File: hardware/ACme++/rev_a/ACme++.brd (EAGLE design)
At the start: 72.6 x 47.1 mm, 90 parts, among them J1 AC-PLUG, J2 WIRE_HOLE-14AWG, J3 TC2030-CTX-NL, J4 WIRE_HOLE-14AWG, J5 WIRE_HOLE-14AWG, K1 S216S01F, Q1 STGD5NB120SZT4, Q2 FDV301N, U1 ADE7753, U2 SR086SG-G, U3 TDA3664AT, U4 FM25LBTDFN-8, U5 CC2538, U6 DS2411, U7 TXB0104RGY, X1 ECS-35-17-5PX-TR, X2 EPSON-FA-128, X3 FC-12M32.7680KA-A3

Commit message: thinking about ac lines, tantalum caps
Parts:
- moved R14 0.13 mm to (46.7, 32.4)
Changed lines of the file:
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@@
 <layer number="27" name="tValues" color="7" fill="1" visible="no" active="yes"/>
 <layer number="28" name="bValues" color="7" fill="1" visible="no" active="yes"/>
-<layer number="29" name="tStop" color="7" fill="3" visible="no" active="yes"/>
+<layer number="29" name="tStop" color="7" fill="3" visible="yes" active="yes"/>
 <layer number="30" name="bStop" color="7" fill="6" visible="no" active="yes"/>
 <layer number="31" name="tCream" color="7" fill="4" visible="no" active="yes"/>
@@
 <wire x1="71.247" y1="33.909" x2="71.247" y2="36.83" width="0.254" layer="21"/>
 <wire x1="71.247" y1="36.83" x2="68.453" y2="36.83" width="0.254" layer="21"/>
-<text x="61.976" y="26.924" size="1.27" layer="21" font="vector" ratio="12" rot="SR270" align="top-center">N</text>
-<text x="61.976" y="19.939" size="1.27" layer="21" font="vector" ratio="12" rot="SR270" align="top-center">P</text>
+<text x="63.881" y="26.924" size="1.27" layer="21" font="vector" ratio="12" rot="SR270" align="top-center">N</text>
+<text x="63.881" y="19.939" size="1.27" layer="21" font="vector" ratio="12" rot="SR270" align="top-center">P</text>
+<polygon width="0" layer="29" spacing="0.254" pour="hatch">
+<vertex x="40.132" y="28.321"/>
+<vertex x="45.974" y="28.321"/>
+<vertex x="48.895" y="31.242"/>
+<vertex x="55.372" y="31.242"/>
+<vertex x="62.103" y="24.511"/>
+<vertex x="62.103" y="18.923"/>
+<vertex x="60.325" y="18.923"/>
+<vertex x="60.198" y="18.923"/>
+<vertex x="60.198" y="23.876"/>
+<vertex x="54.61" y="29.464"/>
+<vertex x="49.657" y="29.464"/>
+<vertex x="46.736" y="26.543"/>
+<vertex x="40.132" y="26.543"/>
+</polygon>
+<polygon width="0" layer="29" spacing="0.254" pour="hatch">
+<vertex x="39.243" y="32.512"/>
+<vertex x="39.243" y="37.973"/>
+<vertex x="43.561" y="42.291"/>
+<vertex x="44.831" y="41.021"/>
+<vertex x="41.021" y="37.211"/>
+<vertex x="41.021" y="32.512"/>
+<vertex x="39.37" y="32.512"/>
+</polygon>
 </plain>
 <attributes>
@@
 <element name="R12" library="SparkFun-Resistors" package="0805" value="1k" x="57.023" y="32.004" smashed="yes" rot="R270">
 <attribute name="DIGIKEY" value="P16058CT-ND" x="57.023" y="32.004" size="1.778" layer="27" rot="R270" display="off"/>
-<attribute name="NAME" x="57.5945" y="29.337" size="1.016" layer="25" font="vector" ratio="12" rot="R90" align="bottom-center"/>
+<attribute name="NAME" x="55.753" y="31.623" size="1.016" layer="25" font="vector" ratio="12" rot="R270" align="center-right"/>
 <attribute name="VALUE" x="55.626" y="33.02" size="0.4064" layer="27" rot="R270"/>
 </element>
@@
 <element name="C13" library="SparkFun-Passives" package="0805" value="33nF" x="58.801" y="32.004" smashed="yes" rot="R90">
 <attribute name="DIGIKEY" value="478-1389-1-ND" x="58.801" y="32.004" size="1.778" layer="27" rot="R90" display="off"/>
-<attribute name="NAME" x="59.3725" y="29.337" size="1.016" layer="25" font="vector" ratio="12" rot="R90" align="bottom-center"/>
+<attribute name="NAME" x="60.071" y="31.242" size="1.016" layer="25" font="vector" ratio="12" rot="R270" align="center-right"/>
 <attribute name="VALUE" x="60.198" y="30.988" size="0.4064" layer="27" rot="R90"/>
 </element>
 <element name="C22" library="SparkFun-Passives" package="0805" value="33nF" x="36.195" y="40.259" smashed="yes">
 <attribute name="DIGIKEY" value="478-1389-1-ND" x="36.195" y="40.259" size="1.778" layer="27" display="off"/>
-<attribute name="NAME" x="34.925" y="38.5445" size="1.016" layer="25" font="vector" ratio="12"/>
+<attribute name="NAME" x="36.195" y="39.5605" size="1.016" layer="25" font="vector" ratio="12" align="top-center"/>
 <attribute name="VALUE" x="35.179" y="38.862" size="0.4064" layer="27"/>
 </element>
 <element name="L4" library="powercube" package="35F0102" value="35F0121-0SR-10" x="51.308" y="33.02" smashed="yes" rot="R180">
 <attribute name="DIGIKEY" value="240-2520-1-ND" x="51.308" y="33.02" size="1.778" layer="27" rot="R180" display="off"/>
-<attribute name="NAME" x="51.308" y="31.115" size="1.016" layer="25" font="vector" ratio="12" rot="R180" align="bottom-center"/>
+<attribute name="NAME" x="51.308" y="34.671" size="1.016" layer="25" font="vector" ratio="12" align="bottom-center"/>
 <attribute name="VALUE" x="51.308" y="36.195" size="1.016" layer="27" font="vector" ratio="12" rot="R180" align="bottom-center"/>
 </element>
-<element name="R14" library="SparkFun-Resistors" package="0805" value="499k" x="46.736" y="32.512" smashed="yes" rot="R270">
-<attribute name="DIGIKEY" value="P499KCCT-ND" x="46.736" y="32.512" size="1.778" layer="27" rot="R270" display="off"/>
-<attribute name="NAME" x="47.3075" y="29.972" size="1.016" layer="25" font="vector" ratio="12" rot="R90" align="bottom-center"/>
-<attribute name="VALUE" x="45.339" y="33.528" size="0.4064" layer="27" rot="R270"/>
+<element name="R14" library="SparkFun-Resistors" package="0805" value="499k" x="46.736" y="32.385" smashed="yes" rot="R270">
+<attribute name="DIGIKEY" value="P499KCCT-ND" x="46.736" y="32.385" size="1.778" layer="27" rot="R270" display="off"/>
+<attribute name="NAME" x="45.593" y="31.115" size="1.016" layer="25" font="vector" ratio="12" rot="R270" align="center-right"/>
+<attribute name="VALUE" x="45.339" y="33.401" size="0.4064" layer="27" rot="R270"/>
 </element>
 <element name="R15" library="SparkFun-Resistors" package="0603-RES" value="1k" x="44.577" y="32.385" smashed="yes" rot="R270">
 <attribute name="DIGIKEY" value="RHM1.00KADCT-ND" x="44.577" y="32.385" size="1.778" layer="27" rot="R270" display="off"/>
-<attribute name="NAME" x="45.085" y="29.718" size="1.016" layer="25" font="vector" ratio="12" rot="R90" align="bottom-center"/>
+<attribute name="NAME" x="44.577" y="31.115" size="1.016" layer="25" font="vector" ratio="12" rot="R90" align="center-right"/>
 <attribute name="VALUE" x="43.434" y="33.401" size="0.4064" layer="27" font="vector" rot="R270"/>
 </element>
 <element name="C23" library="SparkFun-Passives" package="0805" value="33nF" x="42.545" y="32.385" smashed="yes" rot="R90">
 <attribute name="DIGIKEY" value="478-1389-1-ND" x="42.545" y="32.385" size="1.778" layer="27" rot="R90" display="off"/>
-<attribute name="NAME" x="43.1165" y="29.845" size="1.016" layer="25" font="vector" ratio="12" rot="R90" align="bottom-center"/>
+<attribute name="NAME" x="42.545" y="31.115" size="1.016" layer="25" font="vector" ratio="12" rot="R90" align="center-right"/>
 <attribute name="VALUE" x="43.942" y="31.369" size="0.4064" layer="27" rot="R90"/>
 </element>
@@
 <wire x1="31.623" y1="38.227" x2="31.328" y2="37.932" width="0.4064" layer="1"/>
 <wire x1="31.328" y1="37.932" x2="29.535" y2="37.932" width="0.4064" layer="1"/>
-<wire x1="46.736" y1="31.612" x2="46.659" y2="31.535" width="0.762" layer="1"/>
-<wire x1="46.659" y1="31.535" x2="44.577" y2="31.535" width="0.762" layer="1"/>
 <wire x1="44.577" y1="31.535" x2="44.527" y2="31.485" width="0.762" layer="1"/>
 <wire x1="44.527" y1="31.485" x2="42.545" y2="31.485" width="0.762" layer="1"/>
@@
 <via x="32.893" y="38.227" extent="1-16" drill="0.254"/>
 <wire x1="32.893" y1="38.227" x2="31.623" y2="38.227" width="0.4064" layer="1"/>
+<wire x1="44.577" y1="31.535" x2="44.627" y2="31.485" width="0.762" layer="1"/>
+<wire x1="44.627" y1="31.485" x2="46.736" y2="31.485" width="0.762" layer="1"/>
 </signal>
 <signal name="!ADE_CS">
@@
 <contactref element="L4" pad="2"/>
 <contactref element="R14" pad="1"/>
-<wire x1="49.5173" y1="33.02" x2="49.1253" y2="33.412" width="0.762" layer="1"/>
-<wire x1="49.1253" y1="33.412" x2="46.736" y2="33.412" width="0.762" layer="1"/>
+<wire x1="49.5173" y1="33.02" x2="49.2523" y2="33.285" width="0.762" layer="1"/>
+<wire x1="49.2523" y1="33.285" x2="46.736" y2="33.285" width="0.762" layer="1"/>
 </signal>
 <signal name="EARTH_GND">

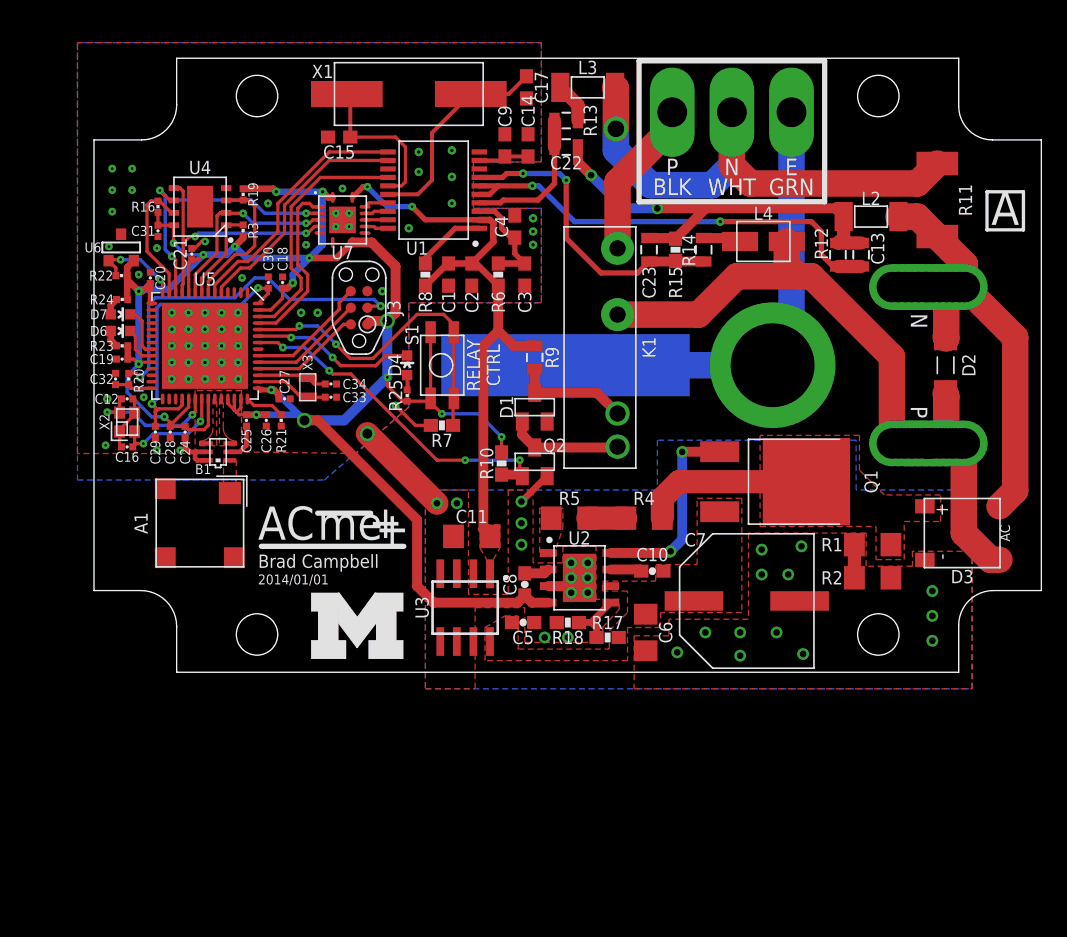
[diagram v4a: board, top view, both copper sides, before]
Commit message: routed ac under board, renamed
did my thing where part numbers correspond to values
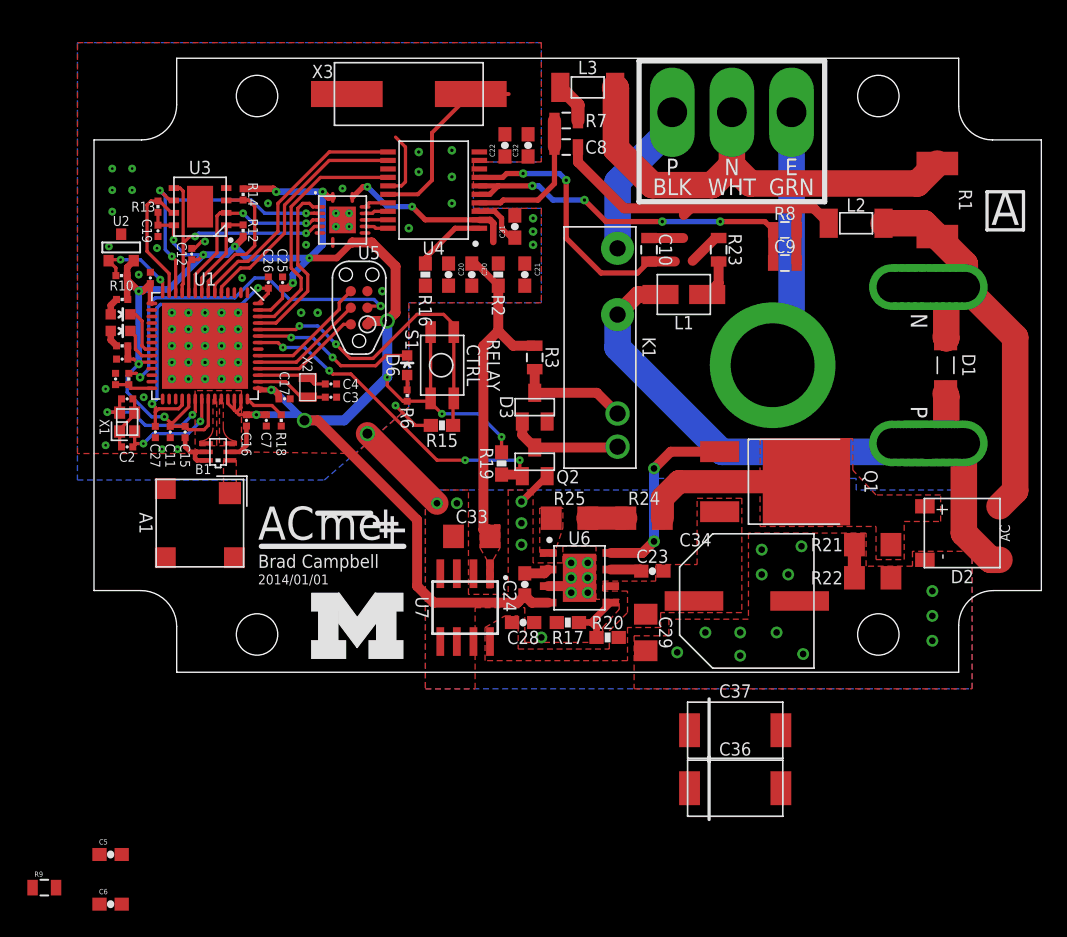
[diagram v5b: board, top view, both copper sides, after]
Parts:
- removed L4: 35F0121-0SR-10, powercube:35F0102
- added C36, C37: (no value), powercube:2917
- added L1: 35F0121-0SR-10, powercube:35F0102
- C1: value 0.1uF -> 12pF; device rcl:C0603 -> passives:0402_CAP
- C10, C8: value 0.1uF -> 33nF; device SparkFun-Passives:0603-CAP -> SparkFun-Passives:0805
- C11: value 47uF -> 0.1uF; device SparkFun-Passives:1206 -> passives:0402_CAP
- C12, C16: value 12pF -> 0.1uF
- C13: value 33nF -> 0.1uF; device SparkFun-Passives:0805 -> passives:0402_CAP
- C14: value 10uF -> 0.1uF; device rcl:C0603 -> passives:0402_CAP
- C15, C17: value 22pF -> 0.1uF; device rcl:C0603 -> passives:0402_CAP
- C18: value 1uF -> 0.1uF
- C2: value 10uF -> 12pF; device rcl:C0603 -> passives:0402_CAP
- C20, C21, C24: device passives:0402_CAP -> SparkFun-Passives:0603-CAP
- C22, C23: value 33nF -> 0.1uF; device SparkFun-Passives:0805 -> SparkFun-Passives:0603-CAP
- C25, C27: value 0.1uF -> 1uF
- C26: value 220pF -> 1uF
- C28: value 0.1uF -> 1uF; device passives:0402_CAP -> SparkFun-Passives:0603-CAP
- C29: device passives:0402_CAP -> SparkFun-Passives:1206
- C3: value 0.1uF -> 22pF; device rcl:C0603 -> passives:0402_CAP
- C30: value 1uF -> 10uF; device passives:0402_CAP -> SparkFun-Passives:0603-CAP
- C31: value 0.1uF -> 10uF; device passives:0402_CAP -> SparkFun-Passives:0603-CAP
- C32: value 1nF -> 10uF; device passives:0402_CAP -> SparkFun-Passives:0603-CAP
- C33: value 22pF -> 47uF; device passives:0402_CAP -> SparkFun-Passives:1206
- C34: value 22pF -> 470uF; device passives:0402_CAP -> powercube:CAP_SM_10MM
- C4: value 10uF -> 22pF; device rcl:C0603 -> passives:0402_CAP
- C5: value 1uF -> 22pF
- C6: value 1uF -> 22pF; device SparkFun-Passives:1206 -> SparkFun-Passives:0603-CAP
- C7: value 470uF -> 220pF; device powercube:CAP_SM_10MM -> passives:0402_CAP
- C9: value 0.1uF -> 33nF; device rcl:C0603 -> SparkFun-Passives:0805
- D1: value DIODE_MMBD914 -> SMAJ_TVS; device powercube:SOT-23 -> powercube:DO214_TVS
- D2: value SMAJ_TVS -> CD2320-BB11000; device powercube:DO214_TVS -> powercube:CD2320
- D3: value CD2320-BB11000 -> DIODE_MMBD914; device powercube:CD2320 -> powercube:SOT-23
- D4: value GREEN -> RED
- D6: value RED -> BLUE
- J2: value WIRE_HOLE-14AWG -> TC2030-CTX-NL; device powercube:WIRE_HOLE-14AWG -> connector:TC2030-IDC-NL
- J3: value TC2030-CTX-NL -> WIRE_HOLE-14AWG; device connector:TC2030-IDC-NL -> powercube:WIRE_HOLE-14AWG
- R1: value 200k -> 0.001; device SparkFun-Resistors:1206 -> SparkFun-Resistors:R2512
- R10: value 100k -> 2.2k; device SparkFun:0603-RES -> passives:0402_RES
- R11: value .001 -> 2.2k; device SparkFun-Resistors:R2512 -> passives:0402_RES
- R12, R13: value 1k -> 4.7k; device SparkFun-Resistors:0805 -> passives:0402_RES
- R14: value 499k -> 4.7k; device SparkFun-Resistors:0805 -> passives:0402_RES
- R15: value 1k -> 10k; device SparkFun-Resistors:0603-RES -> SparkFun:0603-RES
- R16: value 4.7k -> 10k; device passives:0402_RES -> SparkFun:0603-RES
- R17: value 113k -> 12.4k
- R18: value 12.4k -> 56k; device SparkFun-Resistors:0603-RES -> passives:0402_RES
- R19: value 4.7k -> 100k; device passives:0402_RES -> SparkFun:0603-RES
- R2: value 200k -> 10; device SparkFun-Resistors:1206 -> SparkFun:0603-RES
- R20: value 2.2k -> 113k; device passives:0402_RES -> SparkFun-Resistors:0603-RES
- R21: value 56k -> 200k; device passives:0402_RES -> SparkFun-Resistors:1206
- R22: value 2.2k -> 200k; device passives:0402_RES -> SparkFun-Resistors:1206
- R23: value 470 -> 499k; device passives:0402_RES -> SparkFun-Resistors:0805
- R24, R25: value 470 -> 510k; device passives:0402_RES -> SparkFun-Resistors:1206
- R3: value 4.7k -> 330; device passives:0402_RES -> SparkFun-Resistors:0805
- R4, R5: value 510k -> 470; device SparkFun-Resistors:1206 -> passives:0402_RES
- R6: value 10 -> 470; device SparkFun:0603-RES -> passives:0402_RES
- R7, R8: value 10k -> 1k; device SparkFun:0603-RES -> SparkFun-Resistors:0805
- R9: value (none) -> 1k
- U1: value ADE7753 -> CC2538; device powercube:SSOP-20 -> chips:S-PVQFN-N56
- U2: value SR086SG-G -> DS2411; device powercube:SR086 -> chips:SOT-23
- U3: value TDA3664AT -> FM25LBTDFN-8; device powercube:SOIC_8 -> chips:TDFN-8
- U4: value FM25LBTDFN-8 -> ADE7753; device chips:TDFN-8 -> powercube:SSOP-20
- U5: value CC2538 -> TXB0104RGY; device chips:S-PVQFN-N56 -> chips:S-PVQFN-N14
- U6: value DS2411 -> SR086SG-G; device chips:SOT-23 -> powercube:SR086
- U7: value TXB0104RGY -> TDA3664AT; device chips:S-PVQFN-N14 -> powercube:SOIC_8
- X1: value ECS-35-17-5PX-TR -> EPSON-FA-128; device powercube:CSM-7X -> crystals:FA-128
- X2: value EPSON-FA-128 -> FC-12M32.7680KA-A3; device crystals:FA-128 -> crystals:FC-12M
- X3: value FC-12M32.7680KA-A3 -> ECS-35-17-5PX-TR; device crystals:FC-12M -> powercube:CSM-7X
- moved R11 63.5 mm to (2.67, 22.5), turned to 270 degrees
- moved R22 62.1 mm to (59.7, 7.24), turned to 180 degrees
- moved R9 55.4 mm to (-3.81, -16.5), turned to 0 degrees
- moved C13 54.5 mm to (4.32, 30.2)
- moved R21 46.3 mm to (59.7, 9.78), turned to 0 degrees
- moved R23 46.3 mm to (47.9, 32.4), turned to 90 degrees
- moved C6 46.0 mm to (1.27, -17.8), turned to 0 degrees
- moved R12 45.6 mm to (11.4, 33.9)
- moved R24 43.4 mm to (42.2, 11.8), turned to 0 degrees
- moved U2 43.3 mm to (2.11, 32.6), turned to 180 degrees
- moved U6 43.3 mm to (37.2, 7.24), turned to 0 degrees
- moved R4 42.1 mm to (2.16, 25.0), turned to 180 degrees
- moved R20 41.7 mm to (39.4, 2.67), turned to 0 degrees
- moved C29 40.6 mm to (42.3, 3.05)
- moved C7 39.3 mm to (13.2, 19.3), turned to 270 degrees
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- renumbered D7 to D5
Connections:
- removed net N$5: C3.1, C4.1, R6.1, U1.3
- new net ADE_AVDD: C21.1, C31.1, R2.1, U4.3
- net !ADE_CS: now also U1.53, U5.2; no longer U5.53, U7.2
- net !ADE_CS_5V: now also U4.17, U5.13; no longer U1.17, U7.13
- net !ADE_IRQ: now also U1.54, U4.14; no longer U1.14, U5.54
- net !ADE_RESET: now also R16.2, U4.1; no longer R8.2, U1.1
- net !FRAM_CS: now also R12.1, U1.8, U3.1; no longer R3.1, U4.1, U5.8
- net !FRAM_HOLD: now also R13.1, U1.13, U3.7; no longer R16.1, U4.7, U5.13
- net !FRAM_WP: now also R14.1, U1.7, U3.3; no longer R19.1, U4.3, U5.7
- net !RESET: now also J2.3, R11.1; no longer J3.3, R20.1
- net 3V3: now also C11.1, C12.1, C13.1, C14.1, C15.1, C16.1, C17.1, C7.1, J2.1, R10.2, R12.2, R13.2, R14.2, R19.1, R4.1, R5.1, R6.1, U1.10, U1.15, U1.24, U1.33, U1.36, U1.39, U1.40, U1.41, U1.43, U1.55, U2.2, U3.8, U5.1, U5.8, U6.4; no longer C18.1, C20.1, C21.1, C26.1, C27.1, C28.1, C31.1, C8.1, J3.1, R10.1, R16.2, R19.2, R22.2, R23.1, R24.1, R25.1, R3.2, U2.4, U4.8, U5.10, U5.15, U5.24, U5.33, U5.36, U5.39, U5.40, U5.41, U5.43, U5.55, U6.2, U7.1, U7.8
- net 5V0: now also C20.1, C30.1, C33.1, R16.1, R2.2, R3.2, U4.2, U5.14, U7.1; no longer C1.1, C11.1, C2.1, R6.2, R8.1, R9.2, U1.2, U3.1, U7.14
- net ADE_CF: now also U1.6, U4.11; no longer U1.11, U5.6
- net ADE_ZX: now also U1.5, U4.12; no longer U1.12, U5.5
- net DC_RECTIFIED: now also D2.3, R21.2, R24.2; no longer D3.3, R1.2, R4.2
- net DS2411: now also R10.1, U1.14, U2.1; no longer R22.1, U5.14, U6.1
- net EARTH_GND: no longer J1.GND_TAB
- net GND: now also C13.2, C22.2, C34.-, C7.2, D2.4, J2.5, R15.1, R17.1, R18.2, R22.1, U1.VSS_QFN, U3.4, U4.10, U4.8, U5.7, U5.THERMALPAD, U6.2, U6.PAD, U7.3, X1.2, X1.4; no longer C34.2, C7.-, C8.2, C9.2, D3.4, J3.5, R18.1, R2.1, R21.2, R7.1, U1.10, U1.8, U2.2, U2.PAD, U3.3, U4.4, U5.VSS_QFN, U7.7, U7.THERMALPAD, X2.2, X2.4
- net GREEN_LED: now also U1.22; no longer U5.22
- net LOAD_NEUTRAL: now also R1.2; no longer R11.2
- net LOAD_PHASE: now also J3.P$1; no longer J2.P$1
- net MISO: now also U1.9, U3.2, U5.4; no longer U4.2, U5.9, U7.4
- net MISO_5V: now also U4.19, U5.11; no longer U1.19, U7.11
- net MOSI: now also U1.11, U3.5, U5.5; no longer U4.5, U5.11, U7.5
- net MOSI_5V: now also U4.20, U5.10; no longer U1.20, U7.10
- net N$1: now also C26.1, C27.1, U1.32, U1.56; no longer C29.1, C30.1, U5.32, U5.56
- net N$10: now also C2.1, U1.35, X1.3; no longer C16.1, U5.35, X2.3
- net N$11: now also C22.1, C32.1, U4.9; no longer C14.1, C9.1, U1.9
- net N$12: now also D6.A, R6.2; no longer D4.A, R25.2
- net N$13: now also D3.3, R3.1; no longer D1.3, R9.1
- net N$15: now also C5.1, U4.16, X3.2; no longer C17.1, U1.16, X1.2
- net N$16: now also R7.1; no longer R13.1
- net N$17: now also L1.2, R23.1; no longer L4.2, R14.1
- net N$18: now also R21.1, R22.2; no longer R1.1, R2.2
- net N$2: now also C18.1, R11.2, U1.28; no longer C32.1, R20.2, U5.28
- net N$20: now also D4.A, R4.2; no longer D6.A, R23.2
- net N$21: now also R24.1, R25.2; no longer R4.1, R5.2
- net N$22: now also R5.2; no longer R24.2
- net N$24: now also C23.2, U6.7; no longer C10.2, U2.7
- net N$26: now also R17.2, R20.1, U6.5; no longer R17.1, R18.2, U2.5
- net N$3: now also C6.1, U4.15, X3.1; no longer C15.1, U1.15, X1.1
- net N$4: now also D3.1; no longer D1.1
- net N$6: now also C4.1, U1.45, X2.2; no longer C34.1, U5.45, X3.2
- net N$7: now also C3.1, U1.44, X2.1; no longer C33.1, U5.44, X3.1
- net N$8: now also R18.1, U1.42; no longer R21.1, U5.42
- net N$9: now also C1.1, U1.34, X1.1; no longer C12.1, U5.34, X2.1
- net RED_LED: now also D4.C, U1.23; no longer D6.C, U5.23
- net RELAY_CTRL: now also R19.2, U1.50; no longer R10.2, U5.50
- net RELAY_LED: now also D6.C, U1.51; no longer D4.C, U5.51
- net RF_N: now also U1.38; no longer U5.38
- net RF_P: now also U1.37; no longer U5.37
- net SCLK: now also U1.12, U3.6, U5.3; no longer U4.6, U5.12, U7.3
- net SCLK_5V: now also U4.18, U5.12; no longer U1.18, U7.12
- net SR086_GATE: now also U6.8; no longer U2.8
- net SR086_VIN: now also R25.1, U6.1; no longer R5.1, U2.1
- net TCK: now also J2.4, U1.47; no longer J3.4, U5.47
- net TDI: now also U1.49; no longer U5.49
- net TDO: now also J2.6, U1.48; no longer J3.6, U5.48
- net TMS: now also J2.2, U1.46; no longer J3.2, U5.46
- net USER_RELAY_CTRL: now also R15.2, U1.52; no longer R7.2, U5.52
- net V1N: now also C9.1, R8.2, U4.5, U4.6; no longer C13.1, R12.2, U1.5, U1.6
- net V1P: now also C8.1, R7.2, U4.4; no longer C22.1, R13.2, U1.4
- net V2P: now also C10.1, R23.2, R9.2, U4.7; no longer C23.1, R14.2, R15.2, U1.7
- net VDC: now also C23.1, C28.1, C29.1, C34.+, R20.2, U6.6, U7.8; no longer C10.1, C5.1, C6.1, C7.+, R17.2, U2.6, U3.8
- net WALL_NEUTRAL: now also D1.CATHODE, D2.2, R1.1; no longer D2.CATHODE, D3.2, R11.1
- net WALL_NEUTRAL_EMI: now also C10.2, C8.2, C9.2, R8.1, R9.1; no longer C13.2, C22.2, C23.2, R12.1, R15.1
- net WALL_PHASE: now also D1.ANODE, D2.1, L1.1; no longer D2.ANODE, D3.1, L4.1
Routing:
- net EARTH_GND: track 35.9 -> 20.0 mm
- net N$5: track 8.34 -> 0.00 mm
- net 5V0: track 46.2 -> 39.3 mm
- net N$3: track 12.1 -> 5.59 mm
- net V1N: track 34.6 -> 28.2 mm, vias 2 -> 4
- net LOAD_NEUTRAL: track 40.6 -> 36.4 mm, vias 1 -> 0
- net N$11: track 3.86 -> 0.00 mm
- net ADE_AVDD: track 0.00 -> 3.71 mm
- net WALL_PHASE: track 54.4 -> 51.0 mm
- net WALL_NEUTRAL_EMI: track 32.6 -> 30.1 mm, vias 2 -> 0
- net N$15: track 16.5 -> 14.6 mm
- net WALL_NEUTRAL: track 36.9 -> 37.8 mm
- net SR086_GATE: track 15.5 -> 14.8 mm
- net GND: vias 87 -> 86

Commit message: routed the new sparkfun resistors
I changed over to all sparkfun so had to swap out some parts
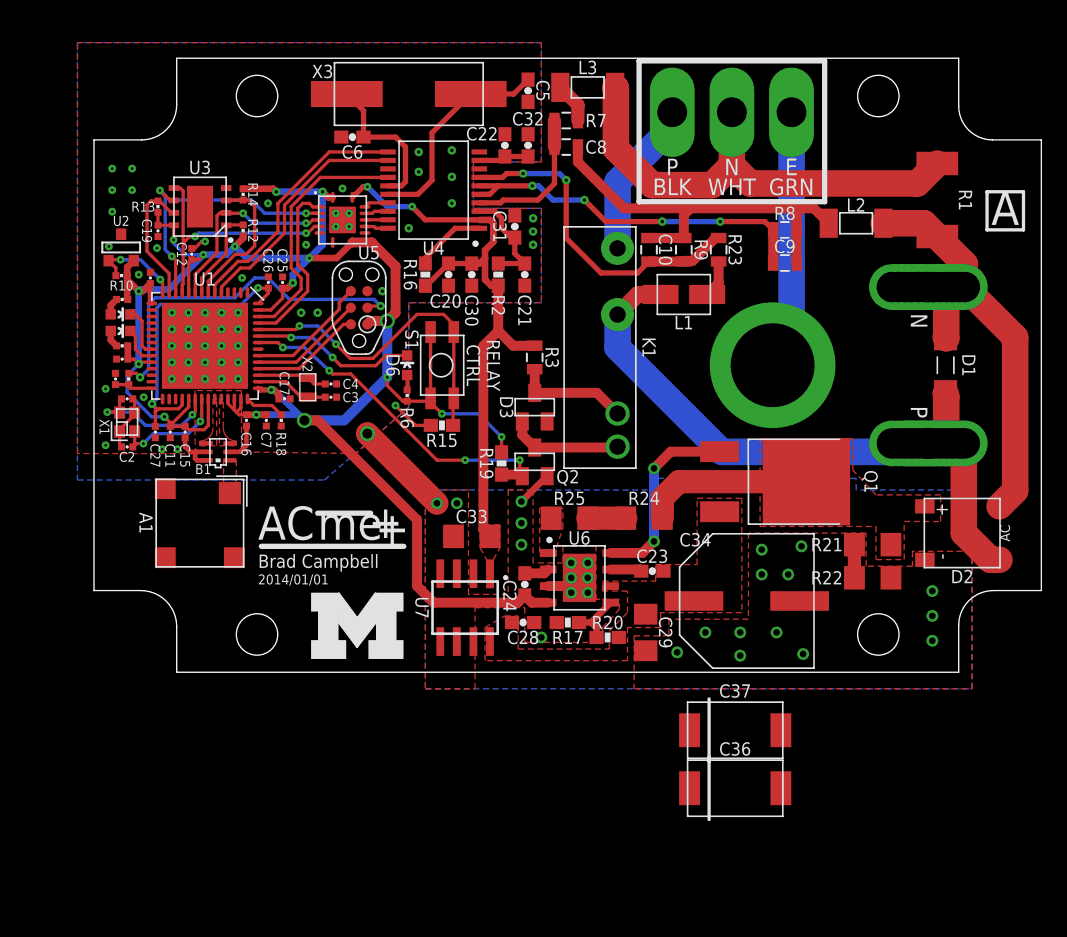
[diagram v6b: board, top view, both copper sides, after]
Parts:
- moved R9 69.2 mm to (45.2, 32.4), turned to 270 degrees
- moved C5 66.7 mm to (33.3, 44.6), turned to 270 degrees
- moved C6 61.7 mm to (19.8, 41.0), turned to 180 degrees
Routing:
- net 5V0: track 39.3 -> 46.7 mm
- net N$3: track 5.59 -> 11.9 mm
- net ADE_AVDD: track 3.71 -> 8.34 mm
- net N$11: track 0.00 -> 3.86 mm
- net N$15: track 14.6 -> 16.5 mm
- net WALL_NEUTRAL_EMI: track 30.1 -> 31.9 mm
- net V2P: track 24.0 -> 25.3 mm
